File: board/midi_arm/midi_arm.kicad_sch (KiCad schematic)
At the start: 32 parts, among them J1 Conn_01x03_Pin, J2 Conn_01x03_Pin, J3 Conn_01x04_Pin, SW1 SW_MEC_5E, SW2 SW_MEC_5E, SW3 SW_MEC_5E, SW4 SW_MEC_5E

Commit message: Bugfixes
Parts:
- R1, R3: value 2.4k -> 33K
- R10, R6: value 3.3k -> DNP
- R11, R12: value 3.3k -> 0
- R13, R14: value 24k -> 51K
- R2, R4: value 5.1k -> 33K
- R5, R7: value 3.3k -> 10K
- R8, R9: value 3.3k -> 33K
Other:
- note added: "Tension Strip Resistance Relaxed = 11.5KOhm"
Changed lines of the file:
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@@
+		)
+	)
+	(text "Tension Strip Resistance Relaxed = 11.5KOhm"
+		(exclude_from_sim no)
+		(at 39.37 160.02 0)
+		(effects
+			(font
+				(size 1.27 1.27)
+			)
 		)
 	)
@@
 		(fields_autoplaced yes)
 		(property "Reference" "R6"
-			(at 40.64 133.2697 90)
-			(effects
-				(font
-					(size 1.27 1.27)
-				)
-			)
-		)
-		(property "Value" "3.3k"
-			(at 40.64 135.6939 90)
+			(at 40.64 133.2695 90)
+			(effects
+				(font
+					(size 1.27 1.27)
+				)
+			)
+		)
+		(property "Value" "DNP"
+			(at 40.64 135.6938 90)
 			(effects
 				(font
@@
 			)
 		)
-		(property "Value" "3.3k"
+		(property "Value" "10K"
 			(at 46.228 125.6721 0)
 			(effects
@@
 		(fields_autoplaced yes)
 		(property "Reference" "R13"
-			(at 87.63 62.1497 90)
-			(effects
-				(font
-					(size 1.27 1.27)
-				)
-			)
-		)
-		(property "Value" "24k"
-			(at 87.63 64.5739 90)
+			(at 87.63 62.1495 90)
+			(effects
+				(font
+					(size 1.27 1.27)
+				)
+			)
+		)
+		(property "Value" "51K"
+			(at 87.63 64.5738 90)
 			(effects
 				(font
@@
 			)
 		)
-		(property "Value" "3.3k"
+		(property "Value" "10K"
 			(at 37.338 123.1321 0)
 			(effects
@@
 		(fields_autoplaced yes)
 		(property "Reference" "R14"
-			(at 87.63 79.9297 90)
-			(effects
-				(font
-					(size 1.27 1.27)
-				)
-			)
-		)
-		(property "Value" "24k"
-			(at 87.63 82.3539 90)
+			(at 87.63 79.9295 90)
+			(effects
+				(font
+					(size 1.27 1.27)
+				)
+			)
+		)
+		(property "Value" "51K"
+			(at 87.63 82.3538 90)
 			(effects
 				(font
@@
 		(fields_autoplaced yes)
 		(property "Reference" "R10"
-			(at 49.53 130.7297 90)
-			(effects
-				(font
-					(size 1.27 1.27)
-				)
-			)
-		)
-		(property "Value" "3.3k"
-			(at 49.53 133.1539 90)
+			(at 49.53 130.7295 90)
+			(effects
+				(font
+					(size 1.27 1.27)
+				)
+			)
+		)
+		(property "Value" "DNP"
+			(at 49.53 133.1538 90)
 			(effects
 				(font
@@
 		(fields_autoplaced yes)
 		(property "Reference" "R12"
-			(at 77.47 79.9297 90)
-			(effects
-				(font
-					(size 1.27 1.27)
-				)
-			)
-		)
-		(property "Value" "3.3k"
-			(at 77.47 82.3539 90)
+			(at 77.47 79.9295 90)
+			(effects
+				(font
+					(size 1.27 1.27)
+				)
+			)
+		)
+		(property "Value" "0"
+			(at 77.47 82.3538 90)
 			(effects
 				(font
@@
 		(fields_autoplaced yes)
 		(property "Reference" "R1"
-			(at 34.29 58.3397 90)
-			(effects
-				(font
-					(size 1.27 1.27)
-				)
-			)
-		)
-		(property "Value" "2.4k"
-			(at 34.29 60.7639 90)
+			(at 34.29 58.3395 90)
+			(effects
+				(font
+					(size 1.27 1.27)
+				)
+			)
+		)
+		(property "Value" "33K"
+			(at 34.29 60.7638 90)
 			(effects
 				(font
@@
 		(fields_autoplaced yes)
 		(property "Reference" "R3"
-			(at 34.29 76.1197 90)
-			(effects
-				(font
-					(size 1.27 1.27)
-				)
-			)
-		)
-		(property "Value" "2.4k"
-			(at 34.29 78.5439 90)
+			(at 34.29 76.1195 90)
+			(effects
+				(font
+					(size 1.27 1.27)
+				)
+			)
+		)
+		(property "Value" "33K"
+			(at 34.29 78.5438 90)
 			(effects
 				(font
@@
 		(fields_autoplaced yes)
 		(property "Reference" "R4"
-			(at 34.29 85.0097 90)
-			(effects
-				(font
-					(size 1.27 1.27)
-				)
-			)
-		)
-		(property "Value" "5.1k"
-			(at 34.29 87.4339 90)
+			(at 34.29 85.0095 90)
+			(effects
+				(font
+					(size 1.27 1.27)
+				)
+			)
+		)
+		(property "Value" "33K"
+			(at 34.29 87.4338 90)
 			(effects
 				(font
@@
 		(fields_autoplaced yes)
 		(property "Reference" "R11"
-			(at 77.47 62.1497 90)
-			(effects
-				(font
-					(size 1.27 1.27)
-				)
-			)
-		)
-		(property "Value" "3.3k"
-			(at 77.47 64.5739 90)
+			(at 77.47 62.1495 90)
+			(effects
+				(font
+					(size 1.27 1.27)
+				)
+			)
+		)
+		(property "Value" "0"
+			(at 77.47 64.5738 90)
 			(effects
 				(font
@@
 		(fields_autoplaced yes)
 		(property "Reference" "R2"
-			(at 34.29 67.2297 90)
-			(effects
-				(font
-					(size 1.27 1.27)
-				)
-			)
-		)
-		(property "Value" "5.1k"
-			(at 34.29 69.6539 90)
+			(at 34.29 67.2295 90)
+			(effects
+				(font
+					(size 1.27 1.27)
+				)
+			)
+		)
+		(property "Value" "33K"
+			(at 34.29 69.6538 90)
 			(effects
 				(font
@@
 		(fields_autoplaced yes)
 		(property "Reference" "R8"
-			(at 46.99 58.3397 90)
-			(effects
-				(font
-					(size 1.27 1.27)
-				)
-			)
-		)
-		(property "Value" "3.3k"
-			(at 46.99 60.7639 90)
+			(at 46.99 58.3395 90)
+			(effects
+				(font
+					(size 1.27 1.27)
+				)
+			)
+		)
+		(property "Value" "33K"
+			(at 46.99 60.7638 90)
 			(effects
 				(font
@@
 		(fields_autoplaced yes)
 		(property "Reference" "R9"
-			(at 46.99 76.1197 90)
-			(effects
-				(font
-					(size 1.27 1.27)
-				)
-			)
-		)
-		(property "Value" "3.3k"
-			(at 46.99 78.5439 90)
-			(effects
-				(font
+			(at 46.99 76.1195 90)
+			(effects
+				(font
+					(size 1.27 1.27)
+				)
+			)
+		)
+		(property "Value" "33K"
+			(at 46.99 78.5438 90)
+			(effects
+				(font

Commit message: Board 3.5 and code cleanup
Mini version of Baboi
Remove Tension Strip option 3/4
Remove  Option for Touch pads
Move light control to host software
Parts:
- removed H2, H3, H4: MountingHole, MountingHole:MountingHole_2.2mm_M2, symbol Mechanical:MountingHole
- removed J1: Conn_01x03_Pin, midi_arm:LED_conn, symbol Connector:Conn_01x03_Pin
- removed R10, R6: DNP, Resistor_SMD:R_0805_2012Metric_Pad1.20x1.40mm_HandSolder, symbol Device:R
- removed R11, R12: 0, Resistor_SMD:R_0805_2012Metric_Pad1.20x1.40mm_HandSolder, symbol Device:R
- removed SW2, SW3, SW4: SW_MEC_5E, GPB_Footprints:switch_Simple, symbol Switch:SW_MEC_5E
- added J4: Conn_01x05_Pin, Connector_PinHeader_2.54mm:PinHeader_1x05_P2.54mm_Vertical, symbol Connector:Conn_01x05_Pin
- added SW2: SW_DIP_x01, Button_Switch_SMD:SW_Push_SPST_NO_Alps_SKRK, symbol Switch:SW_DIP_x01
- added U4: ~, midi_arm:GY-85, symbol midi_arm:GY-85
- H1: footprint MountingHole:MountingHole_2.2mm_M2 -> MountingHole:MountingHole_2mm; now left out of the parts list
- R15: value 24k -> 0k; now not fitted
- R16: value 24k -> 24K; now not fitted
- SW1: footprint GPB_Footprints:switch_Simple -> midi_arm:SW_Push_SMD
- U1: footprint Package_DIP:DIP-8_W7.62mm -> Package_SO:SOIC-8_3.9x4.9mm_P1.27mm
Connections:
- net BUTTON1: now also SW1.1; no longer SW1.2
- net BUTTON2: now also SW2.1
- net GND1: now also SW1.2, J4.3 (Pin_3), SW2.2, U4.3 (GND); no longer SW1.3 (K)
- net SCL: now also U4.4 (SCL)
- net SDA: now also U4.5 (SDA)
- net VCC_3V3: now also U4.2 (3V3)
- net at R5.1: now also J4.2 (Pin_2)
- net at R7.1: now also J4.1 (Pin_1)
- net at R13.1, U1.6 (VinB-): now also R1.2, R8.1
- net at R14.1, U1.2 (VinA-): now also R3.2, R9.1
- net at R15.2, U2.8 (INT): now also U4.7 (A_INT1)
- net BUTTON3 renamed SPARE1
- net SPARE1: now also J4.4 (Pin_4)
- net BUTTON4 renamed SPARE2
- net SPARE2: now also J4.5 (Pin_5)
- no-connect marks 15 -> 12
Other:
- note added: "BOOT"
- note removed: "B"
- note removed: "C"

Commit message: rev 4 board
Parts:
- removed J2: Conn_01x03_Pin, midi_arm:LED_conn, symbol Connector:Conn_01x03_Pin
- removed J3: Conn_01x04_Pin, Connector_PinHeader_2.54mm:PinHeader_1x04_P2.54mm_Vertical, symbol Connector:Conn_01x04_Pin
- removed R15: 0k, Resistor_SMD:R_0805_2012Metric_Pad1.20x1.40mm_HandSolder, symbol Device:R
- removed R16: 24K, Resistor_SMD:R_0805_2012Metric_Pad1.20x1.40mm_HandSolder, symbol Device:R
- added J1: Conn_01x06_Socket, Connector_PinHeader_2.54mm:PinHeader_1x06_P2.54mm_Vertical, symbol Connector:Conn_01x06_Socket
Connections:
- net GND1: now also J1.3 (Pin_3)
- net VBUS: now also J1.1 (Pin_1)
- net VCC_3V3: now also J1.6 (Pin_6)
- net at D2.2 (DOUT): now also J1.2 (Pin_2)
- net at U3.15 (GPIO20): now also J1.4 (Pin_4)
- net at U3.16 (GPIO21): now also J1.5 (Pin_5)
- net at U4.7 (A_INT1): no longer U2.8 (INT)
- net at D1.4 (DIN): now also U3.14 (GPIO10)
- no-connect marks 12 -> 14
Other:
- note removed: "ID/UART/EXT"

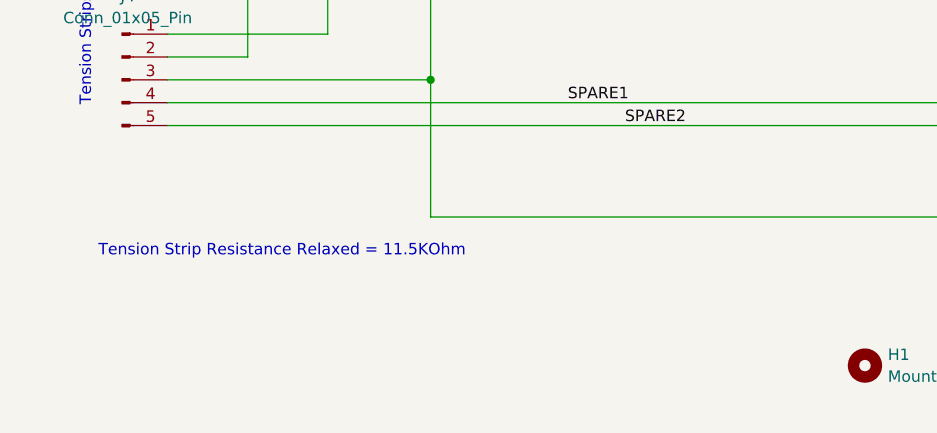
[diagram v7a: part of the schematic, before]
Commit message: Add support for hand detection/add arrow
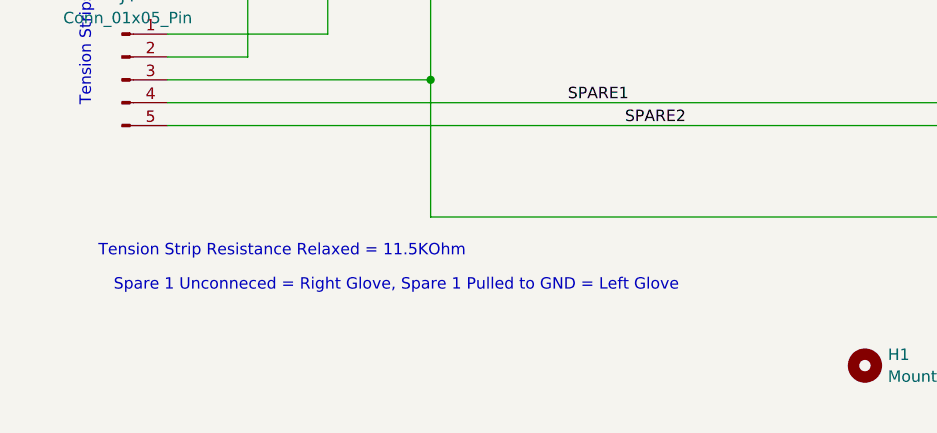
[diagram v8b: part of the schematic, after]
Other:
- note added: "Spare 1 Unconneced = Right Glove, Spare 1 Pulled to GND = Left Glove"
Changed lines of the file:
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@@
+		)
+	)
+	(text "Spare 1 Unconneced = Right Glove, Spare 1 Pulled to GND = Left Glove"
+		(exclude_from_sim no)
+		(at 52.07 163.83 0)
+		(effects
+			(font
+				(size 1.27 1.27)
+			)
 		)
 	)
